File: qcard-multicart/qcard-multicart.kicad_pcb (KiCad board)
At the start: 2 copper layers, 1 part, among them U1 MX29LV640EBTI-70G

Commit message: First pass at multicart
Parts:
- added C1: 1uF, Capacitor_SMD:C_0805_2012Metric_Pad1.18x1.45mm_HandSolder, B.Cu at (79.6, 64.8)
- added C2: 1uF, Capacitor_SMD:C_0805_2012Metric_Pad1.18x1.45mm_HandSolder, B.Cu at (79.6, 62.4)
- added C3: 100pF, Capacitor_SMD:C_0805_2012Metric_Pad1.18x1.45mm_HandSolder, F.Cu at (110.0, 57.5)
- added J1: Conn_02x18_Top_Bottom, reb-edge:REB_EdgeConnector_36pin, F.Cu at (97.0, 75.5)
- added R1: R, Resistor_SMD:R_0805_2012Metric_Pad1.20x1.40mm_HandSolder, B.Cu at (93.2, 49.0)
- added R2: R, Resistor_SMD:R_0805_2012Metric_Pad1.20x1.40mm_HandSolder, B.Cu at (95.7, 49.0)
- added R3: R, Resistor_SMD:R_0805_2012Metric_Pad1.20x1.40mm_HandSolder, B.Cu at (98.3, 49.0)
- added R4: R, Resistor_SMD:R_0805_2012Metric_Pad1.20x1.40mm_HandSolder, B.Cu at (100.8, 49.0)
- added REF**: MountingHole_6.4mm_M6, MountingHole:MountingHole_6.4mm_M6, F.Cu at (74.0, 54.0)
- added REF**: MountingHole_6.4mm_M6, MountingHole:MountingHole_6.4mm_M6, F.Cu at (120.0, 54.0)
- added SW1: SW_DIP_x04, Package_DIP:DIP-8_W7.62mm, F.Cu at (100.8, 36.5)
- added U2: MIC5365-3.3YD5, Package_TO_SOT_SMD:SOT-23-5, B.Cu at (75.4, 63.7)
- moved U1 15.5 mm to (97.0, 58.0)
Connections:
- U1 pad 30: +3.3V -> unconnected-(U1-Pad30)
- U1 pad 32: +3.3V -> unconnected-(U1-Pad32)
- U1 pad 34: +3.3V -> unconnected-(U1-Pad34)
- U1 pad 36: +3.3V -> unconnected-(U1-Pad36)
- U1 pad 39: +3.3V -> unconnected-(U1-Pad39)
- U1 pad 41: +3.3V -> unconnected-(U1-Pad41)
- U1 pad 43: +3.3V -> unconnected-(U1-Pad43)
- U1 pad 47: +3.3V -> GND
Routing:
- net +3.3V: track 0.00 -> 56.0 mm, vias 0 -> 4
- net /A17: track 0.00 -> 40.2 mm, vias 0 -> 1
- net /A10: track 0.00 -> 30.7 mm, vias 0 -> 1
- net GND: track 0.00 -> 28.2 mm, vias 0 -> 4
- net /A16: track 0.00 -> 26.7 mm
- net /A0: track 0.00 -> 26.1 mm
- net /A11: track 0.00 -> 25.9 mm, vias 0 -> 1
- net /A15: track 0.00 -> 25.1 mm
- net /D4: track 0.00 -> 24.9 mm, vias 0 -> 1
- net /D5: track 0.00 -> 24.7 mm, vias 0 -> 1
- net /A14: track 0.00 -> 24.6 mm, vias 0 -> 1
- net /A13: track 0.00 -> 24.6 mm, vias 0 -> 1
- net /D7: track 0.00 -> 23.9 mm, vias 0 -> 1
- net /D6: track 0.00 -> 23.7 mm, vias 0 -> 1
- net Net-(R1-Pad1): track 0.00 -> 23.5 mm, vias 0 -> 1
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- added copper zone on F.Cu, net +3.3V
- added copper zone on B.Cu, net GND
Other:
- board outline added: 55 x 46.5 mm

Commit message: Maybe usable prototype
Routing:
- net +3.3V: track 56.0 -> 106.9 mm, vias 4 -> 2
- net GND: track 28.2 -> 44.4 mm, vias 4 -> 10
- net Net-(R1-Pad1): track 23.5 -> 26.1 mm
- net /A3: track 22.1 -> 24.0 mm
- net /A4: track 20.6 -> 21.6 mm
- added copper zone on F.Cu, net GND
- removed copper zone on F.Cu, net +3.3V
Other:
- rule pad_to_mask_clearance: 0.0508 -> 0

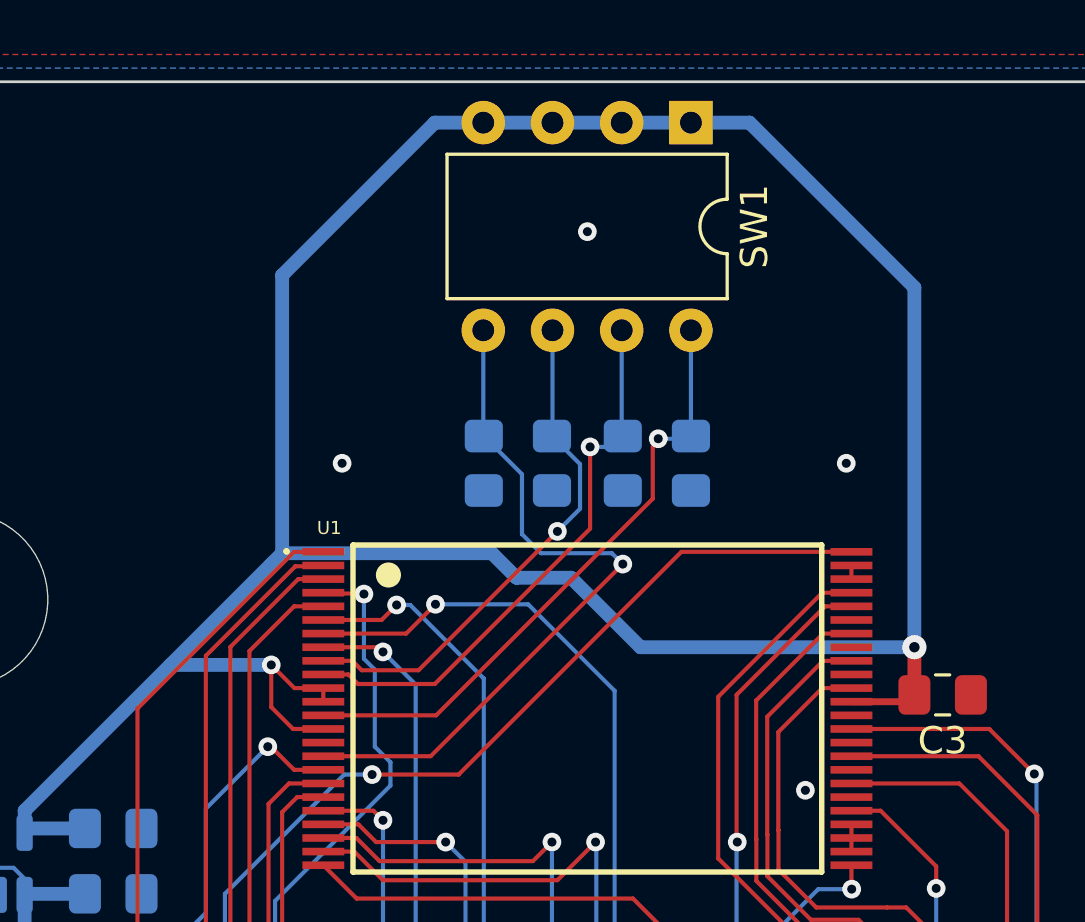
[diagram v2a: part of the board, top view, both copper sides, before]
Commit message: changing pulldown to pullup
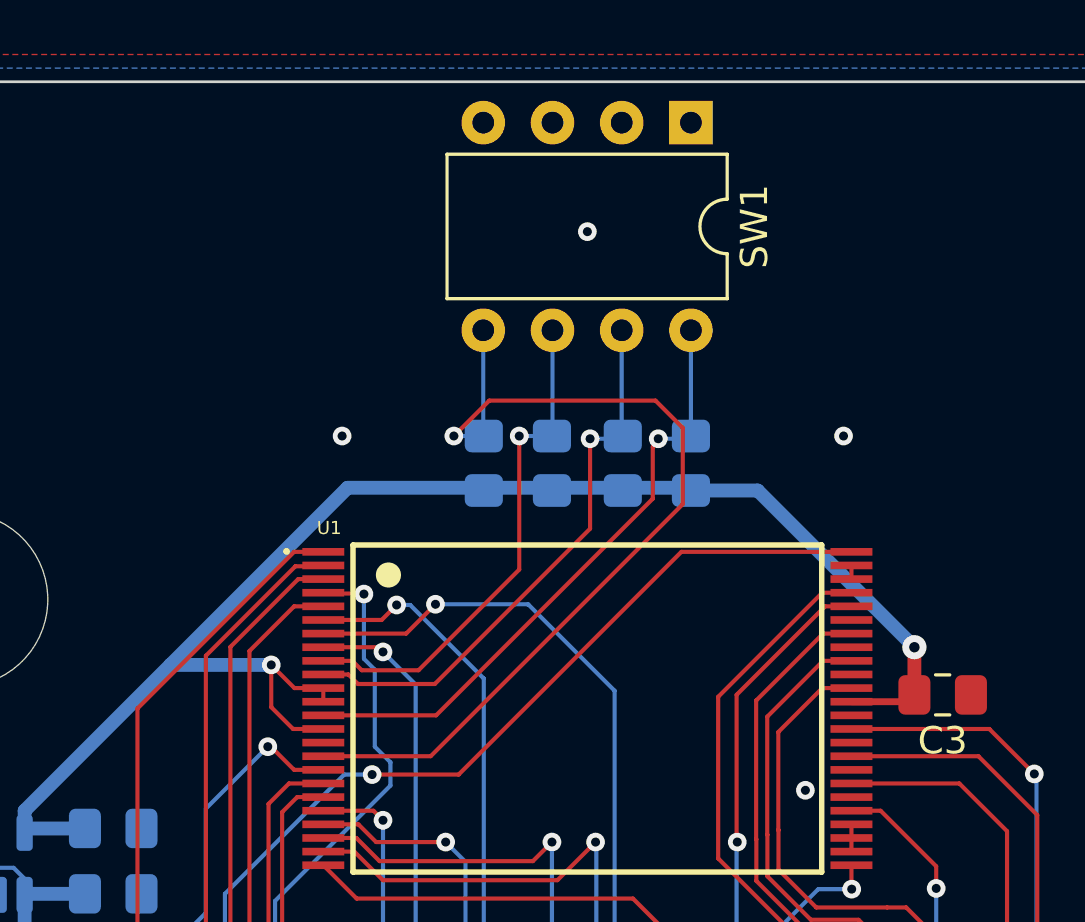
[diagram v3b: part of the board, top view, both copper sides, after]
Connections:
- R1 pad 2: GND -> +3.3V
- R2 pad 2: GND -> +3.3V
- R3 pad 2: GND -> +3.3V
- R4 pad 2: GND -> +3.3V
- SW1 pad 1: +3.3V -> GND
- SW1 pad 2: +3.3V -> GND
- SW1 pad 3: +3.3V -> GND
- SW1 pad 4: +3.3V -> GND
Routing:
- net +3.3V: track 106.9 -> 57.5 mm
- net Net-(R1-Pad1): track 26.1 -> 34.2 mm
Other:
- board text added: "${TITLE} ${COMPANY} ${ISSUE_DATE}"
